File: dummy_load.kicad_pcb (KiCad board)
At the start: 2 copper layers, 16 parts, among them Q1 IRFZ44N

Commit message: Completada la version 1
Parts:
- removed R1: 10k, Resistor_THT:R_Axial_DIN0207_L6.3mm_D2.5mm_P10.16mm_Horizontal
- removed R2: 2k, Resistor_THT:R_Axial_DIN0207_L6.3mm_D2.5mm_P10.16mm_Horizontal
- added C1: 1u, Capacitor_THT:C_Disc_D5.0mm_W2.5mm_P5.00mm, F.Cu at (156.9, 133.3)
- added C2: 100nF, Capacitor_THT:C_Disc_D5.0mm_W2.5mm_P2.50mm, F.Cu at (150.2, 120.0)
- added G***: LOGO, MR-footprint:logo_mr_6x6mm, F.Cu at (168.0, 119.2)
- added H1: MountingHole, MountingHole:MountingHole_3.2mm_M3_Pad_Via, F.Cu at (175.5, 61.0)
- added H2: MountingHole, MountingHole:MountingHole_3.2mm_M3_Pad_Via, F.Cu at (111.0, 61.0)
- added H3: MountingHole, MountingHole:MountingHole_3.2mm_M3_Pad_Via, F.Cu at (111.0, 135.0)
- added H4: MountingHole, MountingHole:MountingHole_3.2mm_M3_Pad_Via, F.Cu at (175.5, 135.0)
- added HS1: Heatsink, MR-footprint:disipador_VGA, F.Cu at (143.8, 86.6)
- added J1: Conn_01x02, Connector_BarrelJack:BarrelJack_Horizontal, F.Cu at (117.5, 123.5)
- added J2: Conn_01x02, TerminalBlock_Phoenix:TerminalBlock_Phoenix_MKDS-1,5-2-5.08_1x02_P5.08mm_Horizontal, F.Cu at (125.5, 133.8)
- added J3: PH_B2B-PH-K, Connector_JST:JST_PH_B2B-PH-K_1x02_P2.00mm_Vertical, F.Cu at (111.5, 110.5)
- added RV1: 5k, Potentiometer_THT:Potentiometer_Alps_RK09Y11_Single_Horizontal, F.Cu at (162.0, 133.5)
- added U1: LM358, Package_DIP:DIP-8_W7.62mm_Socket, F.Cu at (142.6, 123.3)
- Q1: footprint Package_TO_SOT_THT:TO-220-3_Horizontal_TabDown -> Package_TO_SOT_THT:TO-220-3_Horizontal_TabUp
- moved R4 41.2 mm to (153.7, 134.6), turned to 90 degrees
- moved R5 37.8 mm to (148.8, 134.6), turned to 180 degrees
- moved R3 35.4 mm to (130.0, 99.0), turned to 180 degrees
- moved R6 34.7 mm to (139.1, 131.8), turned to 90 degrees
- moved R11 27.8 mm to (157.3, 75.5)
- moved R12 27.8 mm to (157.3, 81.6)
- moved R13 27.8 mm to (157.3, 87.6)
- moved R14 27.8 mm to (157.3, 93.7)
- moved R15 27.8 mm to (157.3, 99.7)
- moved R7 23.8 mm to (129.9, 93.1), turned to 180 degrees
- moved Q1 18.3 mm to (146.4, 96.0), turned to 180 degrees
- moved R10 15.0 mm to (129.9, 75.3), turned to 180 degrees
- moved R8 12.9 mm to (130.0, 87.2), turned to 180 degrees
- moved R9 7.22 mm to (129.9, 81.2), turned to 180 degrees
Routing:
- net /vsense: track 0.00 -> 124.7 mm
- net +12V: track 0.00 -> 85.4 mm, vias 0 -> 3
- net Net-(J2-Pin_1): track 0.00 -> 45.4 mm
- net /vo: track 0.00 -> 33.5 mm
- net /vref: track 0.00 -> 19.5 mm
- net /vin: track 0.00 -> 16.6 mm
- net Net-(U1B--): track 0.00 -> 6.62 mm
- net GND: vias 0 -> 142
- added copper zone on B.Cu, net GND
- added copper zone on F.Cu, net GND
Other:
- board outline added: 72.5 x 82.5 mm
- board text added: "MAYKOLREY.COM DUMB LOAD ${REVISION}"

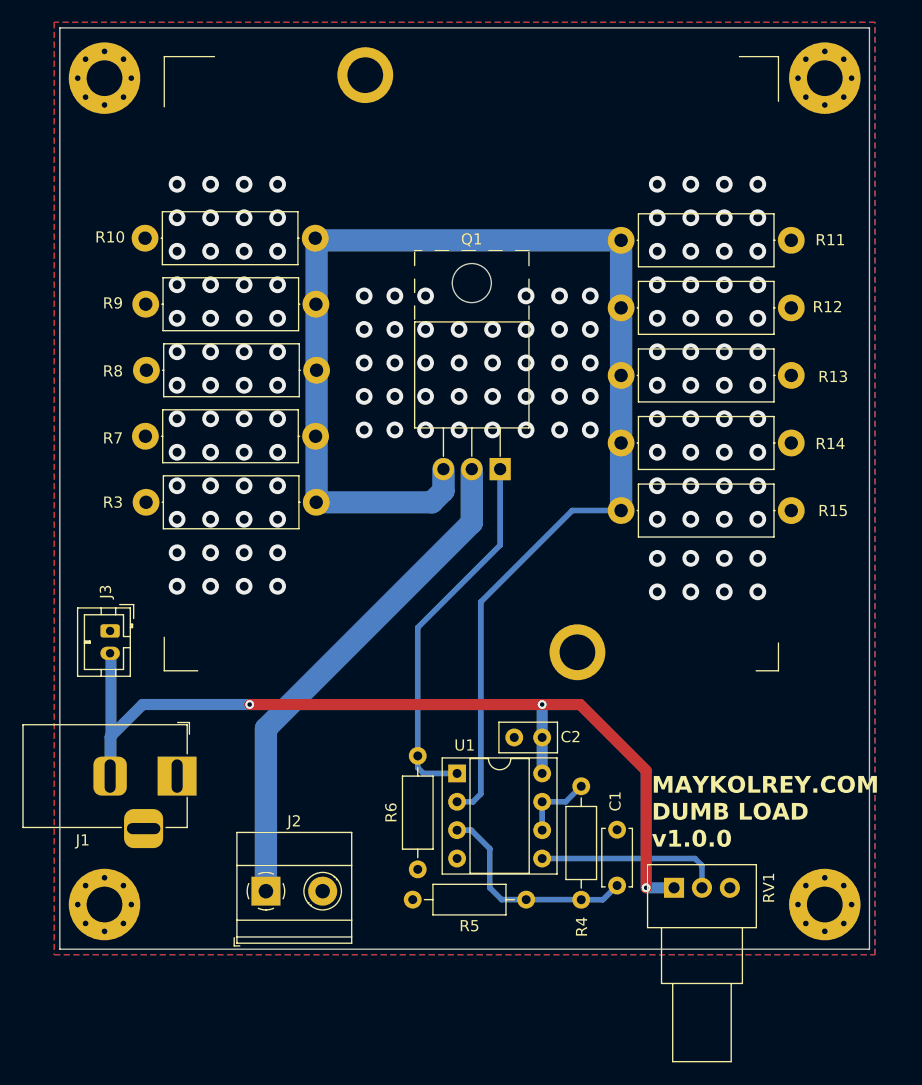
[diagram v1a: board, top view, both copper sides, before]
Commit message: corrigiendo footprint del disipador de calor
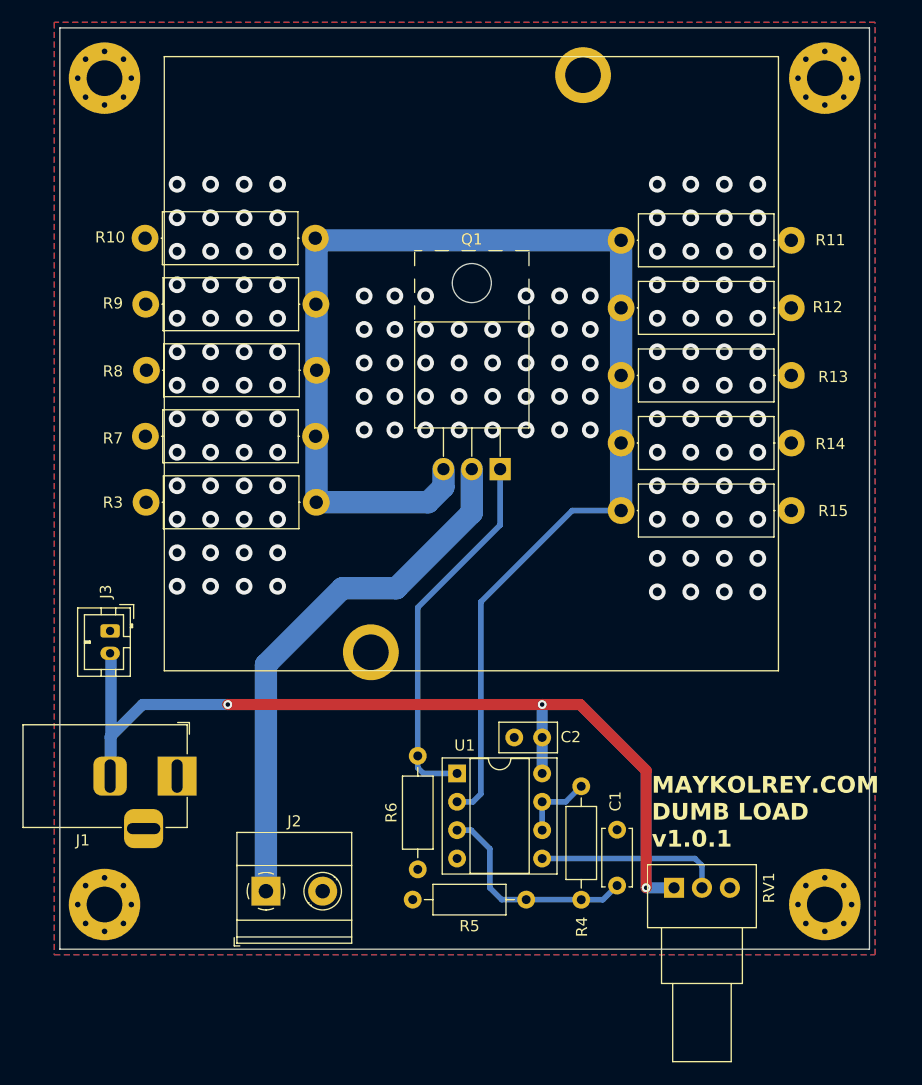
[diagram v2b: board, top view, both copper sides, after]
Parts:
- C1: value 1u -> 1uF
- turned HS1 to -90 degrees
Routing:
- net Net-(J2-Pin_1): track 45.4 -> 48.3 mm

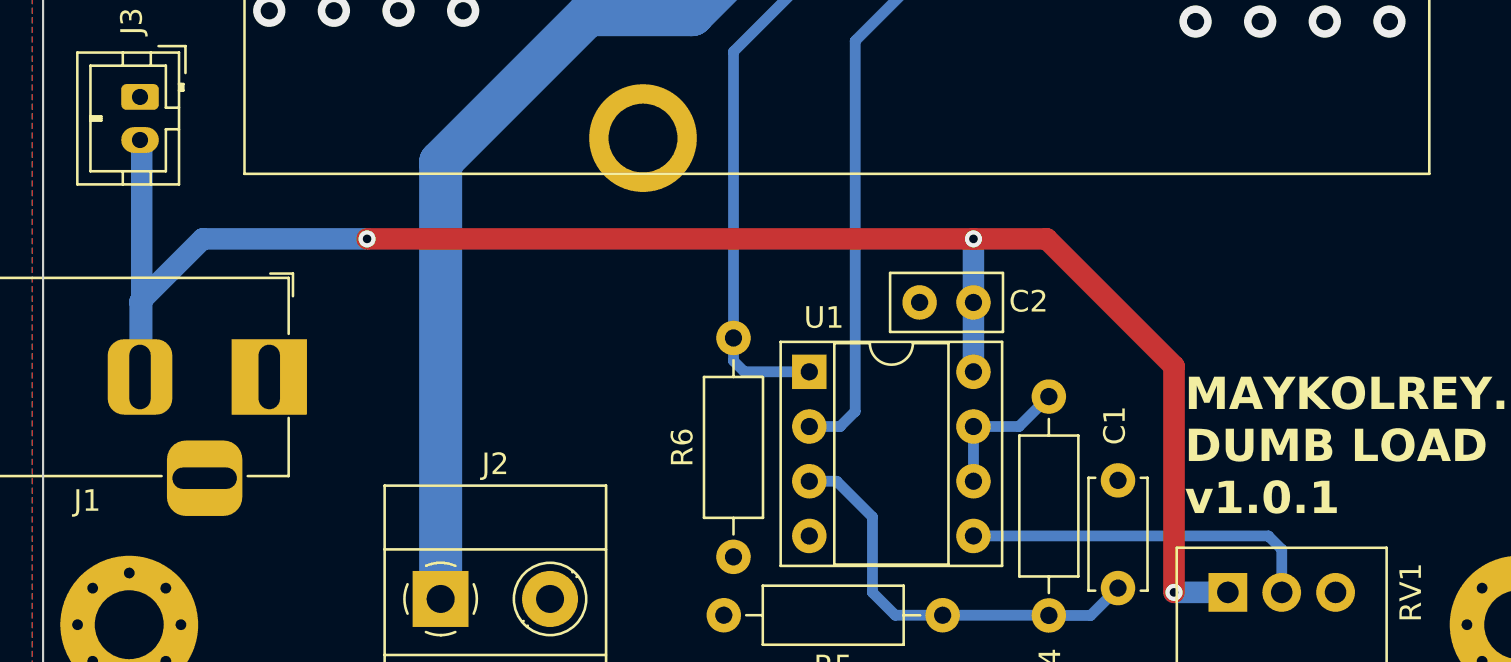
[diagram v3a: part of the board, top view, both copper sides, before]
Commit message: corrigiendo el conector jack-DC invertido
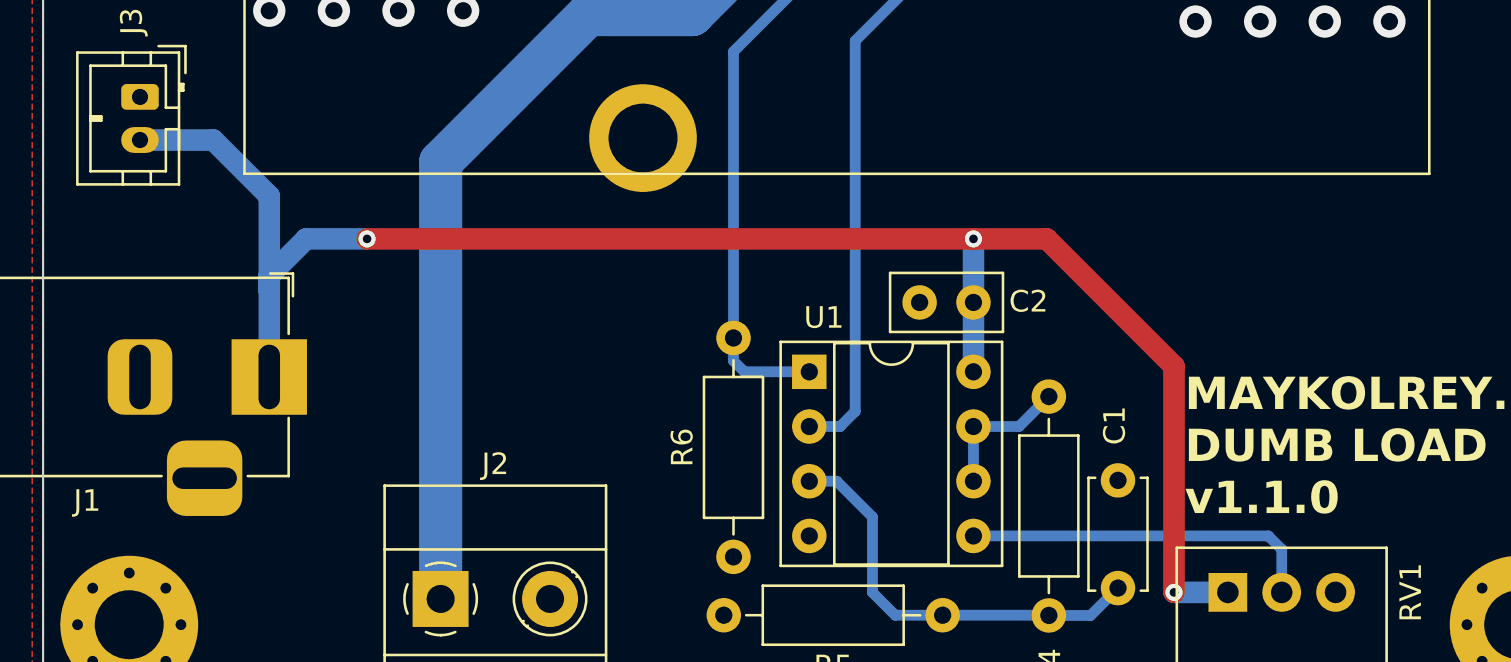
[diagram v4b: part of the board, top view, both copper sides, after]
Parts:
- J1: value Conn_01x02 -> BarrelJack
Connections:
- J1 pad 1: GND -> +12V
- J1 pad 2: +12V -> GND
- J1 pad 3: (no net) -> unconnected-(J1-Pad3)
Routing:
- net +12V: track 85.4 -> 80.5 mm
